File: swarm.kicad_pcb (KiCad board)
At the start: 2 copper layers, 60 x 30 mm, 29 parts, among them P1 USB_OTG, P2 CONN_01X05, P3 CONN_02X20, SW1 SW_PUSH, U1 LM3671MF-3.3, U2 STM32F103RETx, U3 APA102, Y1 Crystal

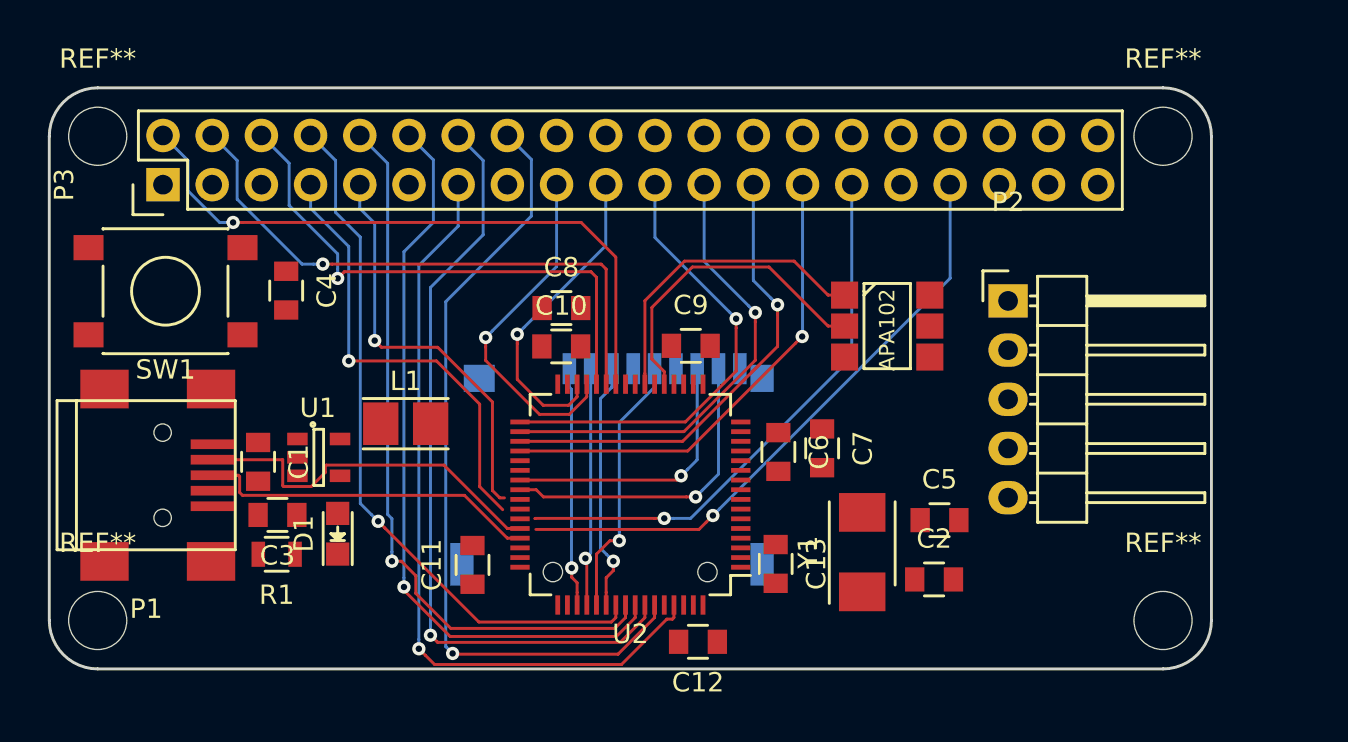
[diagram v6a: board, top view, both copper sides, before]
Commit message: Routed all LCD signals (not LCD_DB9), and capacitos, only power supply left
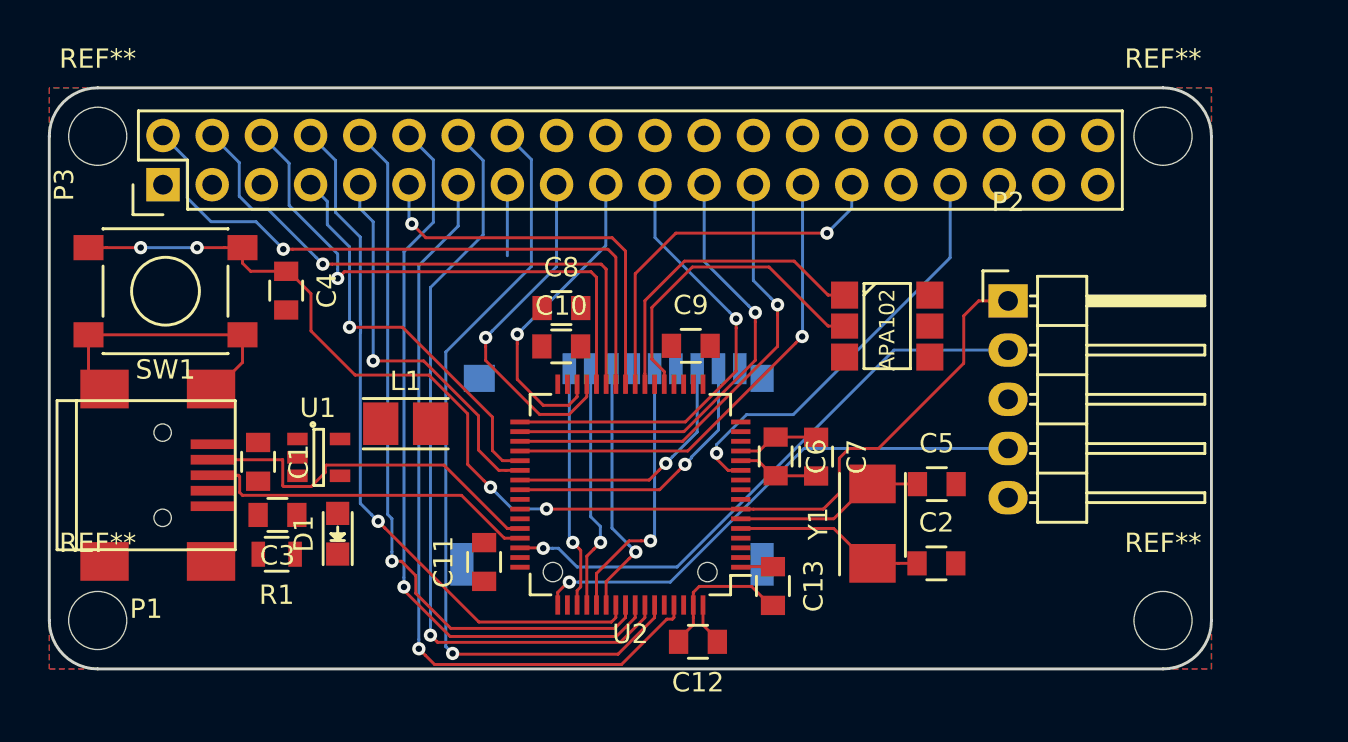
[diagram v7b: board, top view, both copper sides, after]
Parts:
- moved C5 1.87 mm to (145.8, 90.5)
- moved Y1 1.56 mm to (142.5, 92.5)
- moved C13 1.15 mm to (137.4, 95.7)
- moved C2 0.84 mm to (145.8, 94.5)
- moved C11 0.62 mm to (122.5, 94.5)
- moved C7 0.53 mm to (139.6, 89.0)
- moved C6 0.27 mm to (137.5, 89.0)
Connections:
- U2 pad 11: Net-(U2-Pad11) -> /LCD_RST
- U2 pad 24: Net-(U2-Pad24) -> /LCD_CS
- U2 pad 25: Net-(U2-Pad25) -> /LCD_RD
- U2 pad 37: Net-(U2-Pad37) -> /LCD_RS
- U2 pad 38: Net-(U2-Pad38) -> /LCD_WR
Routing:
- net /NRST: track 0.00 -> 63.1 mm, vias 0 -> 4
- net /SWDIO: track 0.00 -> 30.2 mm, vias 0 -> 1
- net /SWCLK: track 0.00 -> 27.0 mm, vias 0 -> 1
- net GND: track 0.00 -> 26.4 mm
- net /LCD_RD: track 0.00 -> 20.6 mm, vias 0 -> 1
- net Net-(C5-Pad1): track 0.00 -> 9.87 mm
- net Net-(C2-Pad1): track 0.00 -> 9.85 mm
- net /LCD_RST: track 31.6 -> 22.1 mm
- net /LCD_CS: track 28.7 -> 19.5 mm
- net +3V3: track 0.00 -> 8.07 mm
- net /LCD_D9: track 0.00 -> 3.67 mm
- net /LCD_RS: track 23.5 -> 20.9 mm
- net /SDIO_D1: track 16.3 -> 14.7 mm
- net /SDIO_D0: track 14.3 -> 13.4 mm
- net /LCD_WR: track 21.1 -> 20.3 mm
- added copper zone on B.Cu, net GND
- added copper zone on F.Cu, net GND

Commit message: Routed all LCD signals
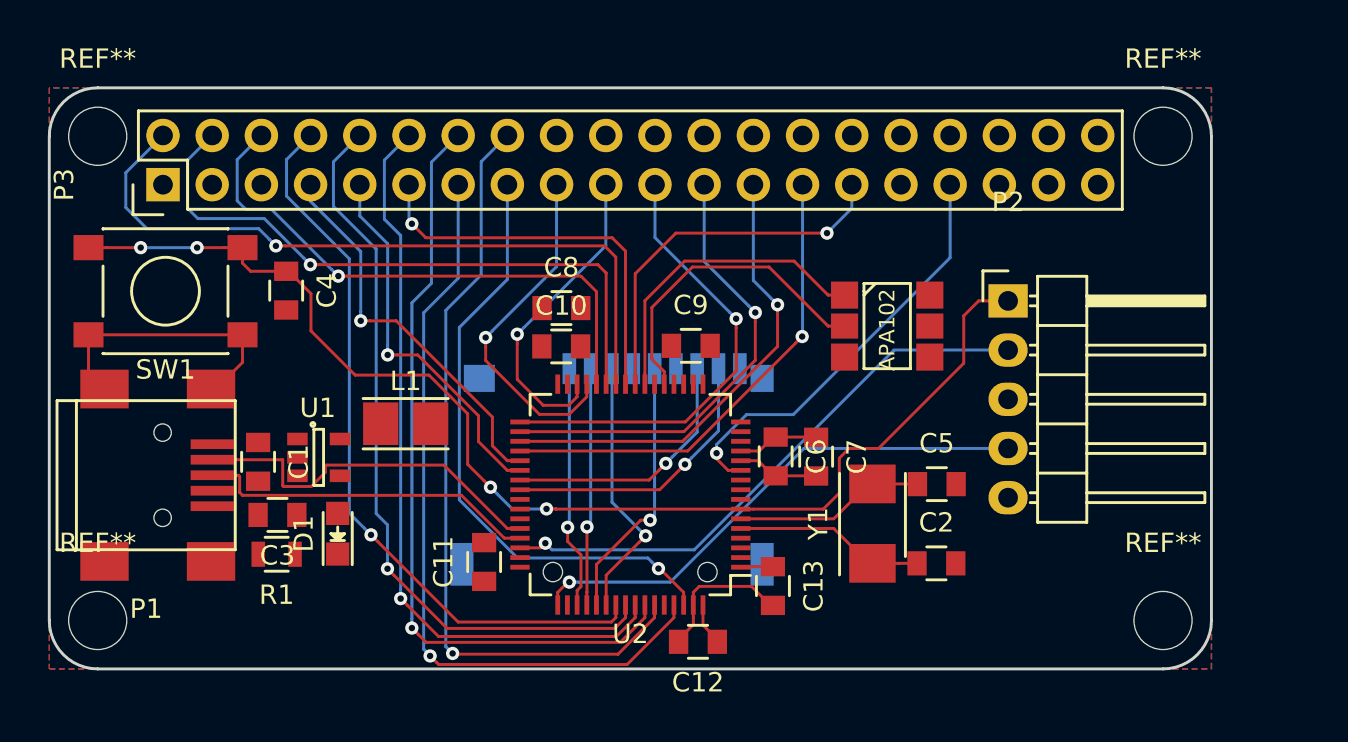
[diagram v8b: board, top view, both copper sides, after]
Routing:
- net /LCD_D9: track 3.67 -> 31.5 mm, vias 0 -> 1
- net /LCD_D0: track 33.7 -> 37.4 mm
- net /LCD_D1: track 30.2 -> 33.0 mm
- net /LCD_D3: track 36.5 -> 38.2 mm
- net /LCD_D7: track 41.1 -> 40.1 mm
- net /LCD_D2: track 28.2 -> 29.2 mm
- net /LCD_D4: track 37.6 -> 38.5 mm
- net /LCD_WR: track 20.3 -> 19.5 mm
- net /LCD_RS: track 20.9 -> 20.2 mm
- net /SWDIO: track 30.2 -> 29.7 mm
